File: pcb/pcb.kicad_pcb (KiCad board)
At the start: 4 copper layers, 52.5 x 52.5 mm, 107 parts, among them CN1 1x4, CN10 1x2, CN11 1x2, CN12 1x8, CN2 1x8, CN3 1x8, CN4 1x8, CN5 1x4, CN6 1x2, CN7 1x2, CN8 1x8, CN9 2x5, IC1 AP2112K-3.3TRG1, IC10 SN74LVC1G17, IC11 SN74LVC1G17, IC12 SN74LVC1G17, IC13 SN74LVC1G17, IC14 SN74LVC1G17, IC15 SN74LVC1G17, IC16 SN74LVC1G17, IC17 SN74LVC1G17, IC18 SN74LVC1G17, IC19 SN74LVC1G17, IC2 STM32f103C8T, IC20 SN74LVC1G17, IC21 SN74LVC1G17, IC22 NPS4053, IC3 INA199B2, IC4 AP62300TWU-7, IC5 MCP2551, IC6 SN74LVC1G17, IC7 SN74LVC1G17, IC8 SN74LVC1G17, IC9 SN74LVC1G17, SW3 219-3LPST

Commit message: worked on layout
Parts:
- moved CN7 60.4 mm to (191.9, 98.1), turned to 0 degrees
- moved CN4 55.9 mm to (166.5, 115.8), turned to 180 degrees
- moved CN3 52.4 mm to (164.0, 115.8), turned to 180 degrees
- moved CN2 48.8 mm to (161.4, 115.8), turned to 180 degrees
- moved C29 38.6 mm to (153.8, 124.1)
- moved IC14 36.9 mm to (157.6, 123.5), turned to 90 degrees
- moved IC15 35.3 mm to (157.6, 120.9), turned to 90 degrees
- moved IC16 34.2 mm to (157.6, 118.4), turned to 90 degrees
- moved C30 34.2 mm to (153.8, 121.6)
- moved IC17 33.6 mm to (157.6, 115.8), turned to 90 degrees
- moved IC18 33.5 mm to (157.6, 113.3), turned to 90 degrees
- moved R3 32.0 mm to (183.0, 110.8)
- moved C31 29.8 mm to (153.8, 119.0)
- moved C32 25.5 mm to (153.8, 116.5)
- moved C33 21.2 mm to (153.8, 113.9)
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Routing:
- net /MCU/CH8: track 26.3 -> 0.00 mm
- net /MCU/CH7: track 24.7 -> 0.00 mm
- net /MCU/CH2: track 24.6 -> 0.00 mm, vias 1 -> 0
- net /MCU/CH6: track 23.0 -> 0.00 mm
- net /MCU/CH5: track 21.3 -> 0.00 mm
- net /MCU/CH1: track 26.6 -> 5.70 mm
- net /MCU/CH4: track 18.3 -> 0.00 mm
- net /MCU/CH3: track 17.8 -> 0.00 mm
- net unconnected-(IC2-OSC_IN-Pad5): track 12.0 -> 0.00 mm
- net unconnected-(IC2-OSC_OUT-Pad6): track 10.1 -> 0.00 mm
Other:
- board text removed: "DFU"
- board text removed: "RESET"

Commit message: worked on layout
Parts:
- added REF**: M3.5, PCB:M3.5, F.Cu at (158.0, 81.0)
- added REF**: M3.5, PCB:M3.5, F.Cu at (158.0, 126.0)
- added REF**: M3.5, PCB:M3.5, F.Cu at (103.0, 81.0)
- added REF**: M3.5, PCB:M3.5, F.Cu at (103.0, 126.0)
- TP1, TP5: moved to B.Cu
- moved TP2 50.6 mm to (181.7, 120.9)
- moved TP3 50.6 mm to (181.7, 118.4)
- moved TP4 50.6 mm to (181.7, 123.5)
- moved CN12 47.5 mm to (120.8, 80.3), turned to 90 degrees
- moved IC6 47.0 mm to (113.2, 86.6), turned to 180 degrees
- moved IC7 44.5 mm to (115.7, 86.6), turned to 180 degrees
- moved CN8 44.4 mm to (120.8, 82.8), turned to 90 degrees
- moved R13 43.6 mm to (112.5, 91.1), turned to -90 degrees
- moved CN4 42.3 mm to (143.6, 80.3), turned to -90 degrees
- moved C9 42.2 mm to (113.8, 91.1), turned to 90 degrees
- moved IC8 42.1 mm to (118.2, 86.6), turned to 180 degrees
- moved R18 40.8 mm to (115.1, 91.1), turned to -90 degrees
- moved IC9 39.9 mm to (120.8, 86.6), turned to 180 degrees
- moved C16 39.5 mm to (116.3, 91.1), turned to 90 degrees
- moved CN3 38.8 mm to (143.6, 82.8), turned to -90 degrees
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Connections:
- CN2 pad 1: /OUT1 -> /output buffers/OUT_1
- CN2 pad 2: /OUT2 -> /output buffers/OUT_2
- CN2 pad 3: /OUT3 -> /output buffers/OUT_3
- CN2 pad 4: /OUT4 -> /output buffers/OUT_4
- CN2 pad 5: /OUT5 -> /output buffers/OUT_5
- CN2 pad 6: /OUT6 -> /output buffers/OUT_6
- CN2 pad 7: /OUT7 -> /output buffers/OUT_7
- CN2 pad 8: /OUT8 -> /output buffers/OUT_8
- IC14 pad 2: /output buffers/CH_1 -> /MCU/CH1
- IC15 pad 2: /output buffers/CH_2 -> /MCU/CH2
- IC16 pad 2: /output buffers/CH_3 -> /MCU/CH3
- IC17 pad 2: /output buffers/CH_4 -> /MCU/CH4
- IC18 pad 2: /output buffers/CH_5 -> /MCU/CH5
- IC19 pad 2: /output buffers/CH_6 -> /MCU/CH6
- IC20 pad 2: /output buffers/CH_7 -> /MCU/CH7
- IC21 pad 2: /output buffers/CH_8 -> /MCU/CH8
- IC22 pad 1: GND -> 5V
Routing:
- net /MCU/NRST: track 40.9 -> 0.00 mm, vias 1 -> 0
- net /MCU/status: track 30.5 -> 0.00 mm, vias 2 -> 0
- net /CAN_H: track 25.7 -> 0.00 mm
- net /MCU/ADDR1: track 25.6 -> 0.00 mm, vias 2 -> 0
- net /MCU/ADDR2: track 23.2 -> 0.00 mm, vias 2 -> 0
- net /MCU/ADDR3: track 21.7 -> 0.00 mm, vias 2 -> 0
- net /CAN_L: track 21.5 -> 0.00 mm
- net /MCU/I_bat: track 29.0 -> 7.93 mm, vias 2 -> 0
- net /MCU/V_bat: track 18.8 -> 0.00 mm, vias 2 -> 0
- net GND: track 17.4 -> 0.00 mm, vias 13 -> 0
- net /MCU/TDO: track 15.5 -> 0.00 mm, vias 1 -> 0
- net 3V3: track 15.4 -> 1.75 mm, vias 11 -> 0
- net 5V: track 12.6 -> 0.00 mm, vias 11 -> 0
- net /MCU/TCK: track 10.6 -> 0.00 mm, vias 1 -> 0
- net /MCU/TDI: track 9.93 -> 0.00 mm, vias 1 -> 0
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- removed copper zone on B.Cu, net /Battery
- removed copper zone on F.Cu, net /power supply/+
- removed copper zone on F.Cu, net 3V3
- removed copper zone on In2.Cu, net 3V3
- removed copper zone on F.Cu, net 5V
- removed copper zone on B.Cu, net Net-(CN6-Pad1)
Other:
- board size 52.5 x 52.5 mm -> 65 x 55 mm
- board text removed: "locked"

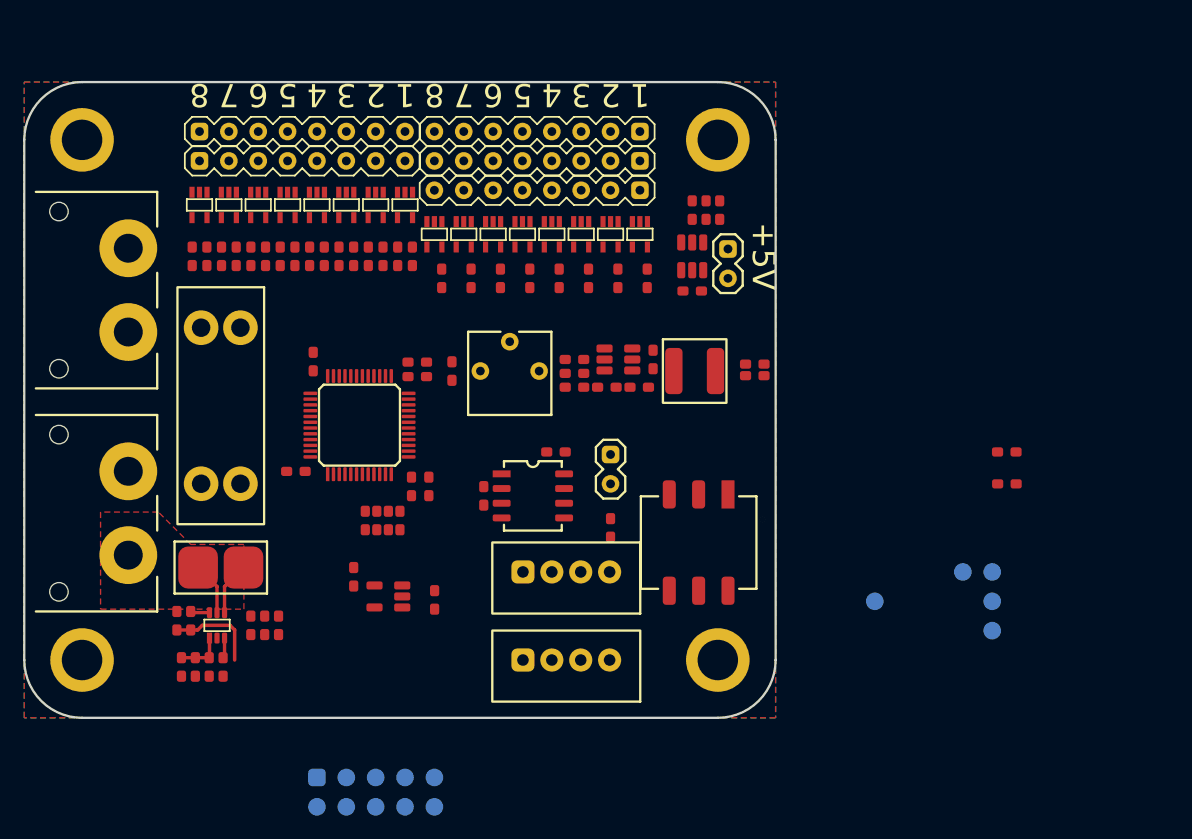
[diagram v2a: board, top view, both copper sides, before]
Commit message: worked on layout. changed step-down module
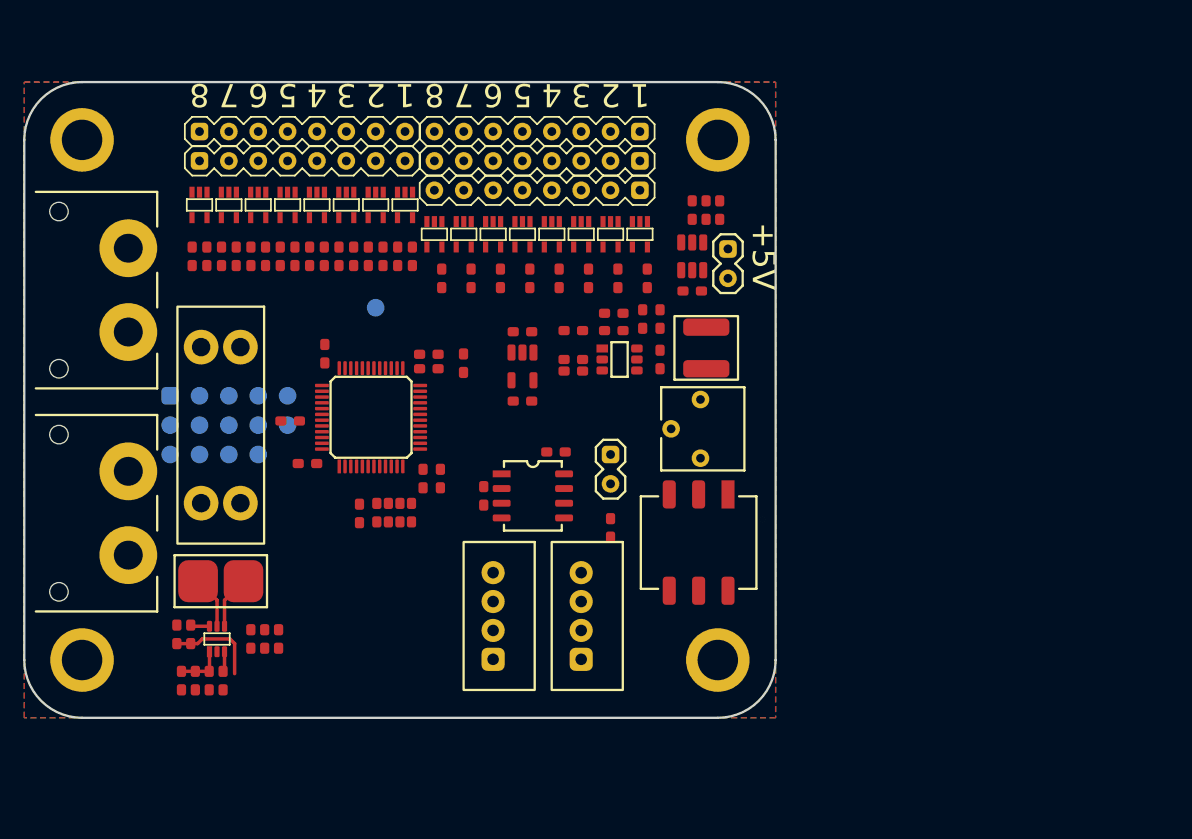
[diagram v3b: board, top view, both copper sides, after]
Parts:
- IC4: value AP62300TWU-7 -> AP63301; footprint SOT:SOT-23-6 -> TSOT:TSOT-26
- moved TP3 71.8 mm to (110.6, 108.2), turned to 90 degrees
- moved TP2 69.7 mm to (113.2, 108.2), turned to 90 degrees
- moved TP4 67.8 mm to (115.7, 108.2), turned to 90 degrees
- moved R12 62.1 mm to (121.0, 105.3)
- moved TP1 61.8 mm to (118.2, 108.2), turned to -90 degrees
- moved R3 56.1 mm to (127.0, 113.3), turned to -90 degrees
- moved TP5 50.1 mm to (128.4, 95.5)
- moved CN9 35.4 mm to (110.6, 103.1)
- moved C1 24.4 mm to (141.1, 97.6), turned to 180 degrees
- moved IC1 23.0 mm to (141.1, 100.6), turned to -90 degrees
- moved C2 21.1 mm to (141.1, 103.6), turned to 180 degrees
- moved R10 17.2 mm to (156.5, 106.0), turned to 90 degrees
- moved C4 10.5 mm to (151.5, 96.5), turned to 90 degrees
- moved C6 9.55 mm to (153.0, 96.5), turned to 90 degrees
- moved CN5 7.39 mm to (138.6, 122.2), turned to 90 degrees
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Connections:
- IC4 pad 1: /Battery -> Net-(IC4-FB)
- IC4 pad 2: Net-(IC4-SW) -> Net-(IC4-EN)
- IC4 pad 3: GND -> /Battery
- IC4 pad 4: Net-(IC4-BST) -> GND
- IC4 pad 5: Net-(IC4-EN) -> Net-(IC4-SW)
- IC4 pad 6: Net-(IC4-FB) -> Net-(IC4-BST)
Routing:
- removed copper zone on F.Cu, net /Battery

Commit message: worked on layout
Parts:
- moved SW3 57.9 mm to (113.0, 77.5), turned to 90 degrees
- moved R10 48.8 mm to (111.0, 123.8), turned to 0 degrees
- moved L1 47.5 mm to (118.2, 126.5), turned to -90 degrees
- moved CN1 44.8 mm to (135.6, 78.6)
- moved CN5 44.8 mm to (128.0, 78.6)
- moved C23 43.2 mm to (113.0, 128.5), turned to 0 degrees
- moved C4 42.8 mm to (122.0, 127.5)
- moved C6 42.8 mm to (123.5, 127.5)
- moved R27 42.8 mm to (145.0, 127.8), turned to -90 degrees
- moved D2 42.1 mm to (146.2, 127.8), turned to 90 degrees
- moved CN7 40.8 mm to (138.2, 128.2), turned to 90 degrees
- moved R15 40.4 mm to (120.0, 75.5), turned to -90 degrees
- moved C21 39.2 mm to (120.5, 122.0), turned to 0 degrees
- moved R26 39.2 mm to (148.0, 125.5), turned to -90 degrees
- moved R17 39.0 mm to (109.0, 128.5), turned to 180 degrees
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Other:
- board size 65 x 55 mm -> 60 x 60 mm
- board text added: "order reversed"
- board text removed: "3.3 V"
- board text removed: "CAN bus"
- board text removed: "battery monitor"
- board text removed: "power supply"

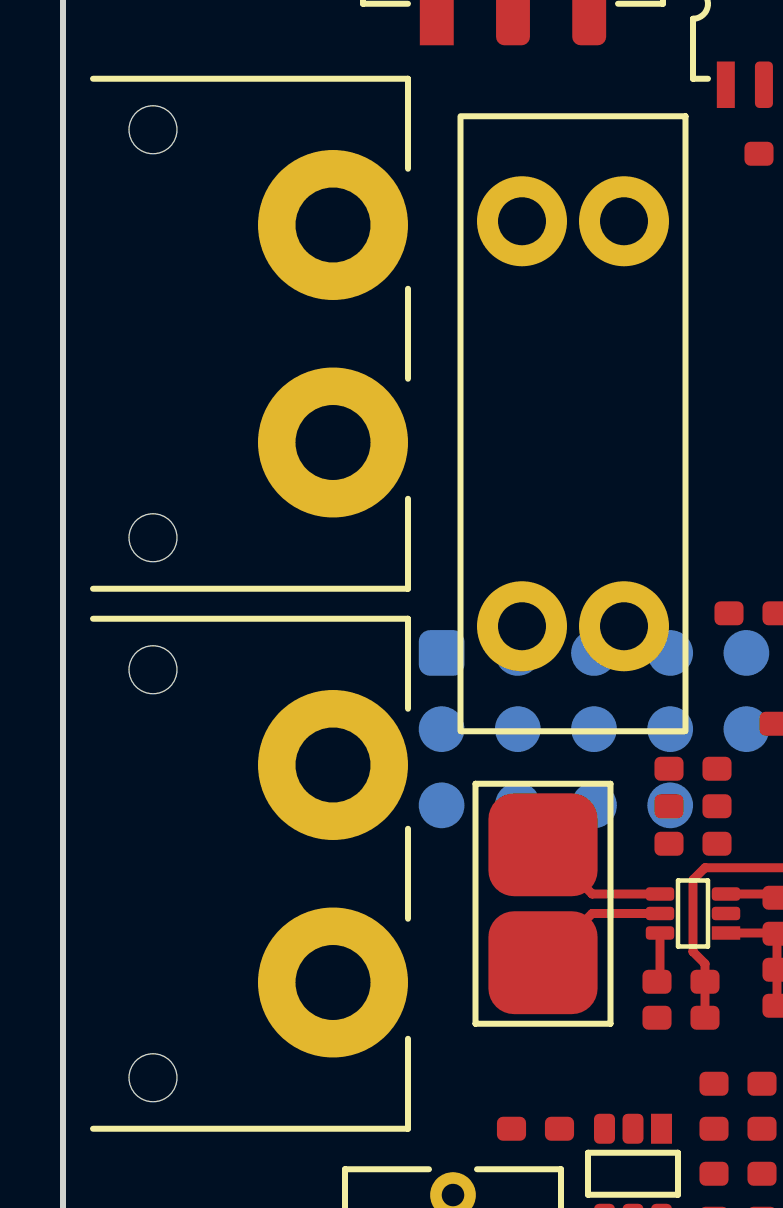
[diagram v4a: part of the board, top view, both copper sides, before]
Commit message: updated xt60 footprint
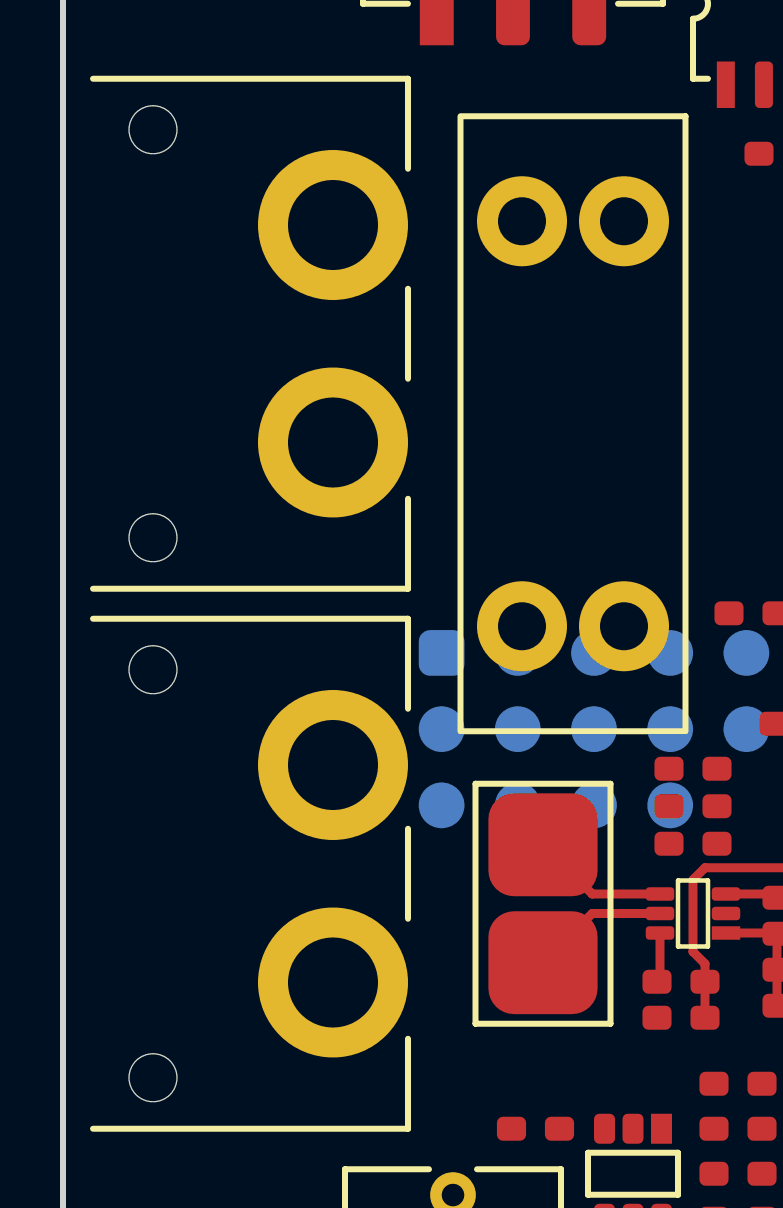
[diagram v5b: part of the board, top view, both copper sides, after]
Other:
- board text removed: "fix via sizes"

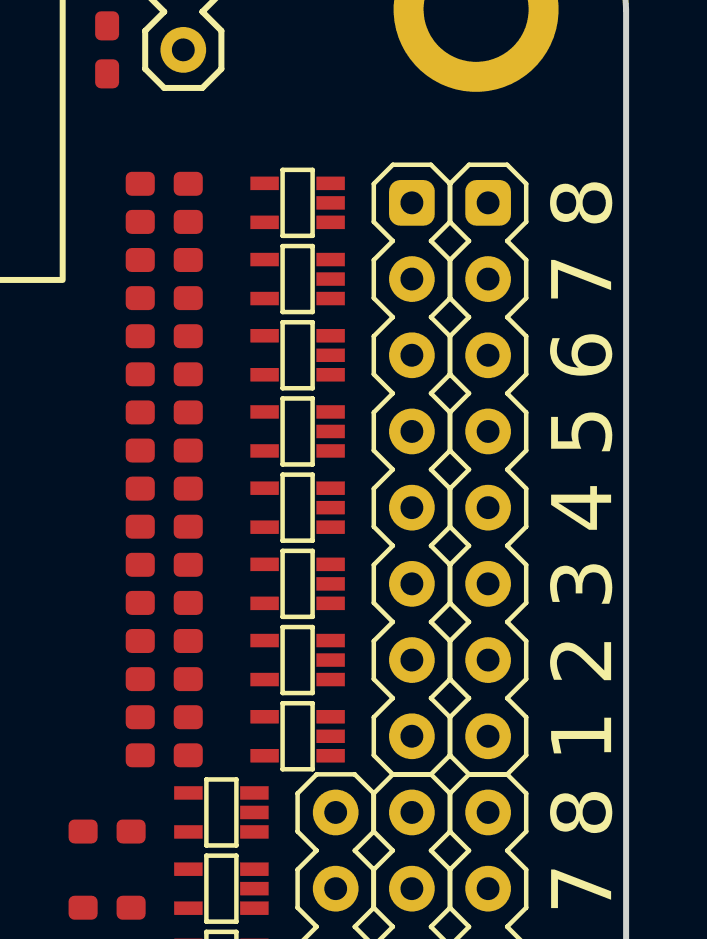
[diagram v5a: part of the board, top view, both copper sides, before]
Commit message: fixed reversed sensor signals
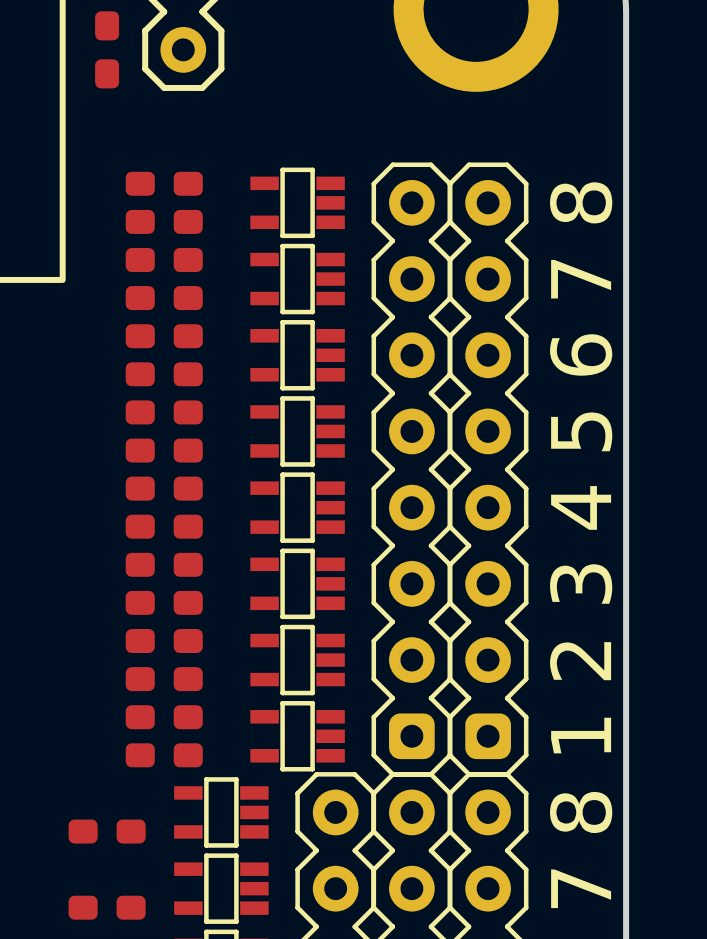
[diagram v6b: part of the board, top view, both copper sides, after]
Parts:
- moved CN12 2.54 mm to (153.4, 92.6), turned to 180 degrees
- moved CN8 2.54 mm to (150.9, 92.6), turned to 180 degrees
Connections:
- CN8 pad 1: /Input  buffers/raw_1 -> /Input  buffers/raw_8
- CN8 pad 2: /Input  buffers/raw_2 -> /Input  buffers/raw_7
- CN8 pad 3: /Input  buffers/raw_3 -> /Input  buffers/raw_6
- CN8 pad 4: /Input  buffers/raw_4 -> /Input  buffers/raw_5
- CN8 pad 5: /Input  buffers/raw_5 -> /Input  buffers/raw_4
- CN8 pad 6: /Input  buffers/raw_6 -> /Input  buffers/raw_3
- CN8 pad 7: /Input  buffers/raw_7 -> /Input  buffers/raw_2
- CN8 pad 8: /Input  buffers/raw_8 -> /Input  buffers/raw_1
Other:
- board text removed: "order reversed"

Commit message: changed CAN driver
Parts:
- IC5: value MCP2551 -> TCAN1057A-Q1; footprint SOP:SO-8 -> TSOT:TSOT-23-8
- moved R4 32.2 mm to (145.0, 76.5), turned to 180 degrees
- moved D1 31.4 mm to (145.0, 78.0), turned to 180 degrees
- moved CN10 17.1 mm to (130.5, 88.8), turned to 90 degrees
- moved R14 13.4 mm to (133.0, 88.3), turned to 90 degrees
- moved IC5 8.06 mm to (123.0, 89.5), turned to 0 degrees
- moved CN5 6.37 mm to (131.8, 83.7), turned to 180 degrees
- moved CN1 4.57 mm to (131.8, 76.1), turned to 180 degrees
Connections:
- IC5 pad 5: unconnected-(IC5-VREF-Pad5) -> (no net)
- IC5 pad 8: Net-(IC5-RS) -> GND

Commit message: worked on layout
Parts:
- moved C1 8.25 mm to (132.0, 121.5)
- moved C2 8.25 mm to (132.0, 115.5)
- moved IC1 8.25 mm to (132.0, 118.5)
- moved C31 4.62 mm to (145.1, 114.8), turned to 180 degrees
- moved C33 4.62 mm to (145.1, 109.8), turned to 180 degrees
- moved C29 4.62 mm to (145.1, 119.9), turned to 180 degrees
- moved C30 4.62 mm to (145.1, 117.4), turned to 180 degrees
- moved C32 4.62 mm to (145.1, 112.3), turned to 180 degrees
- moved C34 4.62 mm to (145.1, 107.2), turned to 180 degrees
- moved C35 4.62 mm to (145.1, 104.7), turned to 180 degrees
- moved C36 4.62 mm to (145.1, 102.1), turned to 180 degrees
- moved IC14 3.17 mm to (141.3, 120.5), turned to -90 degrees
- moved IC15 3.17 mm to (141.3, 118.0), turned to -90 degrees
- moved IC16 3.17 mm to (141.3, 115.5), turned to -90 degrees
- moved IC17 3.17 mm to (141.3, 112.9), turned to -90 degrees
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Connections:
- CN8 pad 1: /Input  buffers/raw_8 -> /Input  buffers/raw_1
- CN8 pad 2: /Input  buffers/raw_7 -> /Input  buffers/raw_2
- CN8 pad 3: /Input  buffers/raw_6 -> /Input  buffers/raw_3
- CN8 pad 4: /Input  buffers/raw_5 -> /Input  buffers/raw_4
- CN8 pad 5: /Input  buffers/raw_4 -> /Input  buffers/raw_5
- CN8 pad 6: /Input  buffers/raw_3 -> /Input  buffers/raw_6
- CN8 pad 7: /Input  buffers/raw_2 -> /Input  buffers/raw_7
- CN8 pad 8: /Input  buffers/raw_1 -> /Input  buffers/raw_8
- IC10 pad 2: /Input  buffers/raw_5 -> /Input  buffers/raw_4
- IC10 pad 4: /Input  buffers/IN_5 -> /Input  buffers/IN_4
- IC11 pad 2: /Input  buffers/raw_6 -> /Input  buffers/raw_3
- IC11 pad 4: /Input  buffers/IN_6 -> /Input  buffers/IN_3
- IC12 pad 2: /Input  buffers/raw_7 -> /Input  buffers/raw_2
- IC12 pad 4: /Input  buffers/IN_7 -> /Input  buffers/IN_2
- IC13 pad 2: /Input  buffers/raw_8 -> /Input  buffers/raw_1
- IC13 pad 4: /Input  buffers/IN_8 -> /Input  buffers/IN_1
- IC6 pad 2: /Input  buffers/raw_1 -> /Input  buffers/raw_8
- IC6 pad 4: /Input  buffers/IN_1 -> /Input  buffers/IN_8
- IC7 pad 2: /Input  buffers/raw_2 -> /Input  buffers/raw_7
- IC7 pad 4: /Input  buffers/IN_2 -> /Input  buffers/IN_7
- IC8 pad 2: /Input  buffers/raw_3 -> /Input  buffers/raw_6
- IC8 pad 4: /Input  buffers/IN_3 -> /Input  buffers/IN_6
- IC9 pad 2: /Input  buffers/raw_4 -> /Input  buffers/raw_5
- IC9 pad 4: /Input  buffers/IN_4 -> /Input  buffers/IN_5
- R13 pad 1: /Input  buffers/raw_1 -> /Input  buffers/raw_8
- R18 pad 1: /Input  buffers/raw_2 -> /Input  buffers/raw_7
- R19 pad 1: /Input  buffers/raw_3 -> /Input  buffers/raw_6
- R20 pad 1: /Input  buffers/raw_4 -> /Input  buffers/raw_5
- R21 pad 1: /Input  buffers/raw_5 -> /Input  buffers/raw_4
- R22 pad 1: /Input  buffers/raw_6 -> /Input  buffers/raw_3
- R23 pad 1: /Input  buffers/raw_7 -> /Input  buffers/raw_2
- R24 pad 1: /Input  buffers/raw_8 -> /Input  buffers/raw_1
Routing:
- net /Servo VCC: track 0.00 -> 53.6 mm, vias 0 -> 16
- net 3V3: track 1.75 -> 31.3 mm, vias 0 -> 8
- net /Input  buffers/raw_8: track 0.00 -> 7.72 mm
- net /Input  buffers/raw_6: track 0.00 -> 7.72 mm
- net /Input  buffers/raw_4: track 0.00 -> 7.72 mm
- net /Input  buffers/raw_3: track 0.00 -> 7.72 mm
- net /Input  buffers/raw_1: track 0.00 -> 7.72 mm
- net /Input  buffers/raw_7: track 0.00 -> 7.72 mm
- net /Input  buffers/raw_5: track 0.00 -> 7.72 mm
- net /Input  buffers/raw_2: track 0.00 -> 7.72 mm
- net /output buffers/OUT_8: track 0.00 -> 6.15 mm
- net /output buffers/OUT_6: track 0.00 -> 6.15 mm
- net /output buffers/OUT_5: track 0.00 -> 6.15 mm
- net /output buffers/OUT_3: track 0.00 -> 6.15 mm
- net /output buffers/OUT_1: track 0.00 -> 6.15 mm
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- added copper zone on In2.Cu, net /Battery
- added copper zone on In2.Cu, net /Servo VCC
- added copper zone on In2.Cu, net 3V3
